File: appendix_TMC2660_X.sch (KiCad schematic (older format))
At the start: 56 parts, among them J601 Conn_01x04, J602 Conn_01x04, J603 Conn_01x04, J604 Conn_01x04, U601 TMC2660, U602 TMC2660, U603 TMC2660, U604 TMC2660

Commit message: started layouting TMC2660
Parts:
- added C633, C634, C635, C636: 470u, Capacitors_SMD:CP_Elec_6.3x5.3, symbol Device:CP
- C601, C604, C607, C608, C609, C610, C611, C612, C613, C614, C615, C616, C617, C620, C623, C624, C625, C626, C627, C628, C629, C630, C631, C632: footprint Capacitors_SMD:C_0805 -> Capacitors_SMD:C_0603
- C602, C603, C605, C606, C618, C619, C621, C622: footprint Capacitors_SMD:C_0805 -> Capacitors_SMD:C_1210
- J601, J602, J603, J604: value Conn_01x04 -> B4B-XH-A; footprint Connector_PinHeader_2.54mm:PinHeader_1x04_P2.54mm_Vertical -> Connector_JST:JST_XH_B4B-XH-A_1x04_P2.50mm_Vertical
- R601, R603, R605, R607, R609, R611, R613, R615: footprint Resistors_SMD:R_0805 -> Resistors_SMD:R_0603
- R602, R604, R606, R608, R610, R612, R614, R616: footprint Resistors_SMD:R_0805 -> Resistors_SMD:R_1210
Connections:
- wire segments 348 -> 364
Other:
- moved on the sheet: J602

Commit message: Layout: all TMC / Schematic: Oli's comments
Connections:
- net labels added: +24V, +3.3V
- net labels removed: +12V
- wire segments 364 -> 372

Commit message: added footprints, layouted 3v3 Reg
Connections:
- net D_INT_TMC_STALL_X: now reaches U602.38 (SG_TST)
- net D_INT_TMC_STALL_Y: now reaches U601.38 (SG_TST)
- net D_INT_TMC_STALL_Z1: now reaches U604.38 (SG_TST)
- net D_INT_TMC_STALL_E1: now reaches U603.38 (SG_TST)
- no-connect marks 0 -> 4

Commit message: added LEDs
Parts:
- C633, C634, C635, C636: footprint Capacitors_SMD:CP_Elec_6.3x5.3 -> Capacitor_SMD:CP_Elec_10x10
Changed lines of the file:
@@
 F 0 "C634" H 6568 1296 50  0000 L CNN
 F 1 "470u" H 6568 1205 50  0000 L CNN
-F 2 "Capacitors_SMD:CP_Elec_6.3x5.3" H 6488 1100 50  0001 C CNN
+F 2 "Capacitor_SMD:CP_Elec_10x10" H 6488 1100 50  0001 C CNN
 F 3 "~" H 6450 1250 50  0001 C CNN
 	1    6450 1250
@@
 F 0 "C633" H 13518 1246 50  0000 L CNN
 F 1 "470u" H 13518 1155 50  0000 L CNN
-F 2 "Capacitors_SMD:CP_Elec_6.3x5.3" H 13438 1050 50  0001 C CNN
+F 2 "Capacitor_SMD:CP_Elec_10x10" H 13438 1050 50  0001 C CNN
 F 3 "~" H 13400 1200 50  0001 C CNN
 	1    13400 1200
@@
 F 0 "C636" H 13518 5946 50  0000 L CNN
 F 1 "470u" H 13518 5855 50  0000 L CNN
-F 2 "Capacitors_SMD:CP_Elec_6.3x5.3" H 13438 5750 50  0001 C CNN
+F 2 "Capacitor_SMD:CP_Elec_10x10" H 13438 5750 50  0001 C CNN
 F 3 "~" H 13400 5900 50  0001 C CNN
 	1    13400 5900
@@
 F 0 "C635" H 6568 5946 50  0000 L CNN
 F 1 "470u" H 6568 5855 50  0000 L CNN
-F 2 "Capacitors_SMD:CP_Elec_6.3x5.3" H 6488 5750 50  0001 C CNN
+F 2 "Capacitor_SMD:CP_Elec_10x10" H 6488 5750 50  0001 C CNN
 F 3 "~" H 6450 5900 50  0001 C CNN
 	1    6450 5900

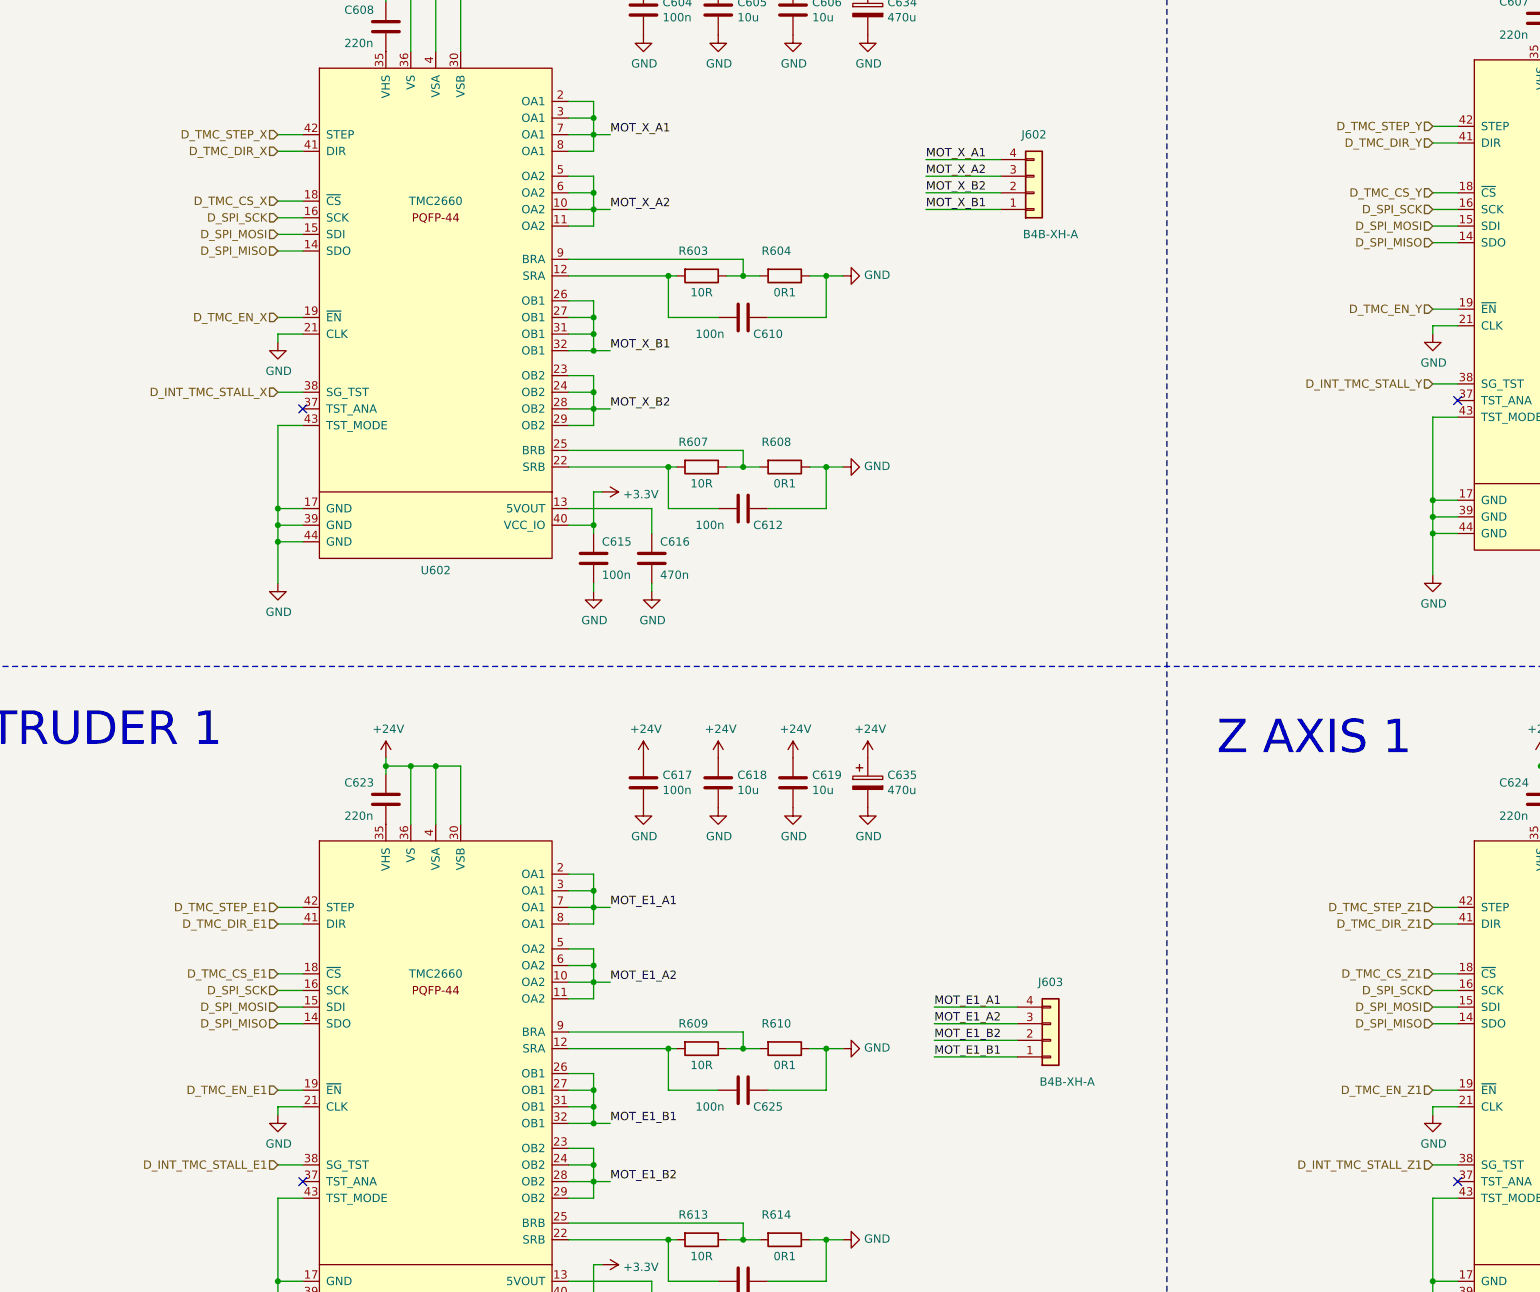
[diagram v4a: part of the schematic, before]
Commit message: started with STM32 Pinout connections (Mittagspause)
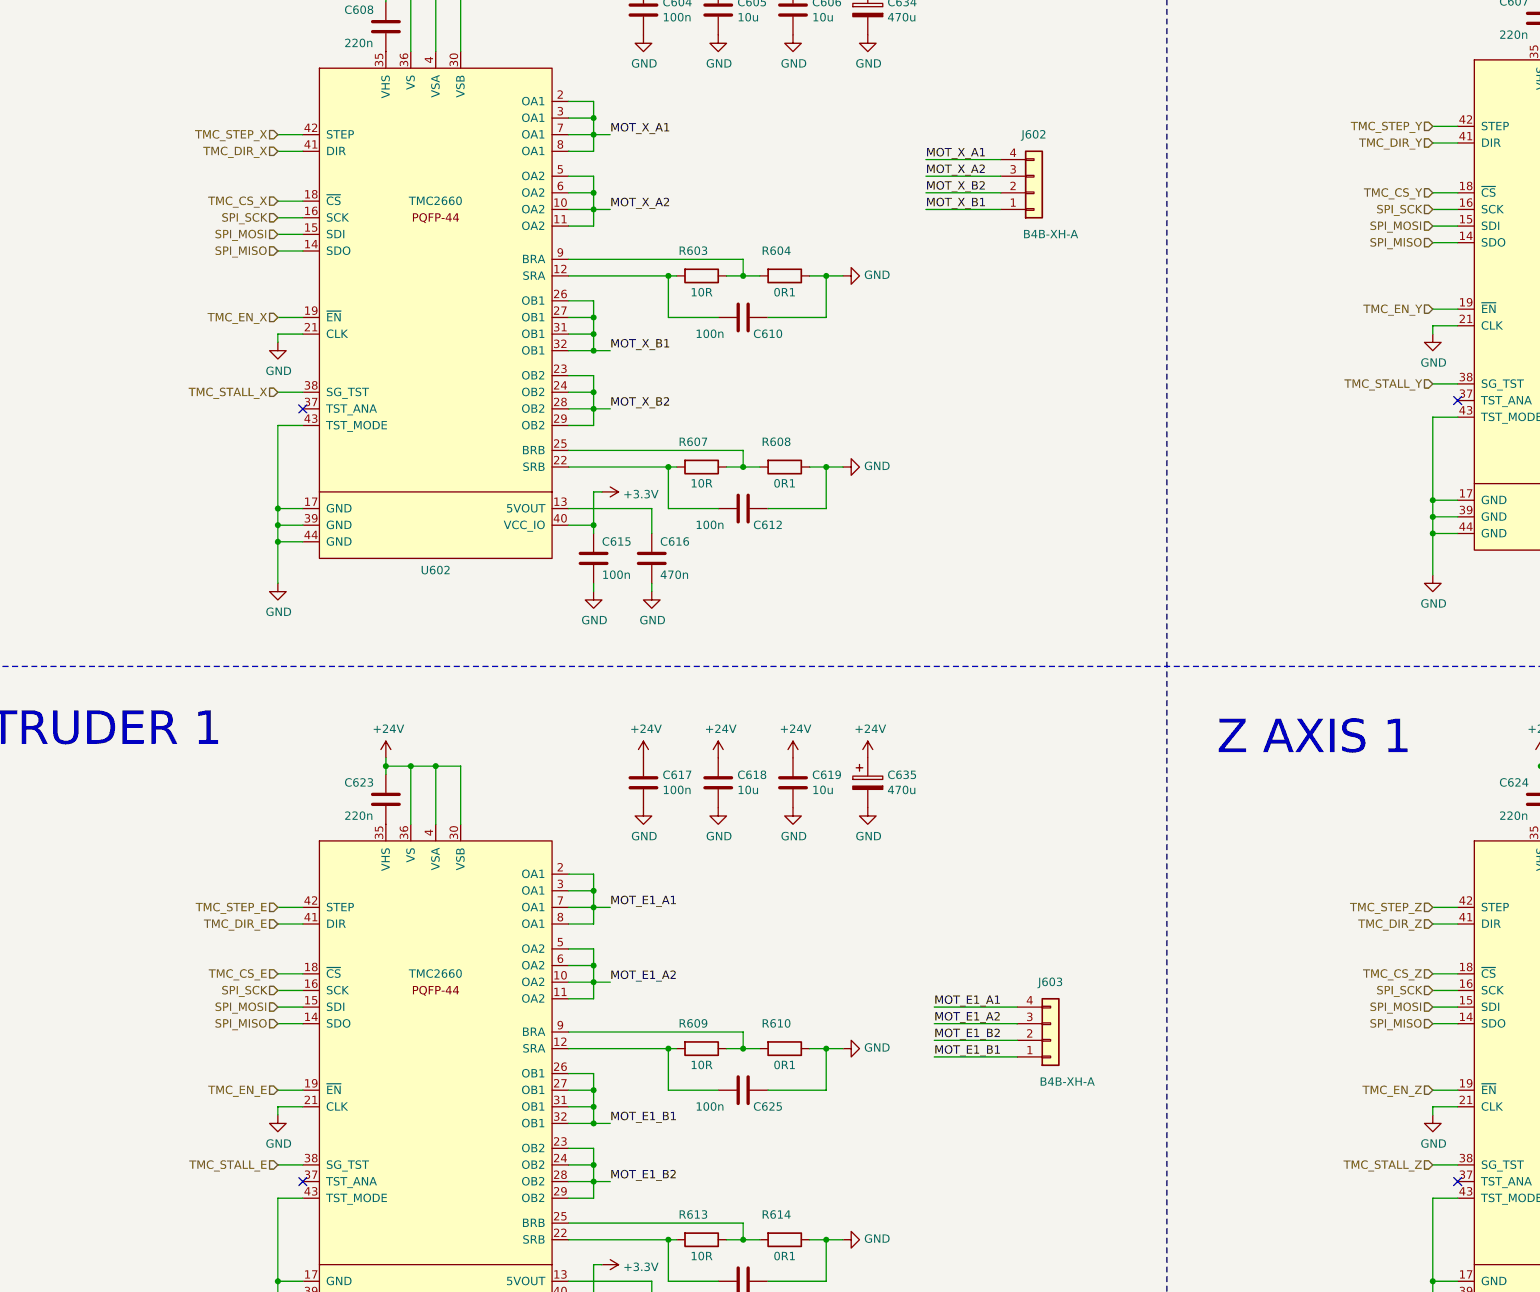
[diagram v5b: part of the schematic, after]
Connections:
- net D_INT_TMC_STALL_E1 renamed TMC_STALL_E
- net D_INT_TMC_STALL_X renamed TMC_STALL_X
- net D_INT_TMC_STALL_Y renamed TMC_STALL_Y
- net D_INT_TMC_STALL_Z1 renamed TMC_STALL_Z
- net D_SPI_MISO renamed SPI_MISO
- net D_SPI_MOSI renamed SPI_MOSI
- net D_SPI_SCK renamed SPI_SCK
- net D_TMC_CS_E1 renamed TMC_CS_E
- net D_TMC_CS_X renamed TMC_CS_X
- net D_TMC_CS_Y renamed TMC_CS_Y
- net D_TMC_CS_Z1 renamed TMC_CS_Z
- net D_TMC_DIR_E1 renamed TMC_DIR_E
- net D_TMC_DIR_X renamed TMC_DIR_X
- net D_TMC_DIR_Y renamed TMC_DIR_Y
- net D_TMC_DIR_Z1 renamed TMC_DIR_Z
- net D_TMC_EN_E1 renamed TMC_EN_E
- net D_TMC_EN_X renamed TMC_EN_X
- net D_TMC_EN_Y renamed TMC_EN_Y
- net D_TMC_EN_Z1 renamed TMC_EN_Z
- net D_TMC_STEP_E1 renamed TMC_STEP_E
- net D_TMC_STEP_X renamed TMC_STEP_X
- net D_TMC_STEP_Y renamed TMC_STEP_Y
- net D_TMC_STEP_Z1 renamed TMC_STEP_Z
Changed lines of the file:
@@
 $Descr A3 16535 11693
 encoding utf-8
-Sheet 6 6
+Sheet 5 6
 Title "TMC2660 Stepper Drivers"
 Date ""
@@
 Wire Wire Line
 	3550 1150 3550 1100
-Text HLabel 2900 3100 0    50   Input ~ 0
-D_TMC_EN_X
 Wire Wire Line
 	3050 3750 2900 3750
@@
 	2900 3750 2900 4250
 Connection ~ 2900 4250
-Text HLabel 2900 2400 0    50   Input ~ 0
-D_TMC_CS_X
-Text HLabel 2900 2500 0    50   Input ~ 0
-D_SPI_SCK
-Text HLabel 2900 2600 0    50   Input ~ 0
-D_SPI_MOSI
-Text HLabel 2900 2700 0    50   Input ~ 0
-D_SPI_MISO
 Wire Wire Line
 	2900 2400 3050 2400
@@
 Wire Wire Line
 	2900 3200 3050 3200
-Text HLabel 2900 2000 0    50   Input ~ 0
-D_TMC_STEP_X
 Wire Wire Line
 	2900 2000 3050 2000
-Text HLabel 2900 2100 0    50   Input ~ 0
-D_TMC_DIR_X
 Wire Wire Line
 	2900 2100 3050 2100
@@
 	1    0    0    -1
 $EndComp
-Text HLabel 9850 3050 0    50   Input ~ 0
-D_TMC_EN_Y
 Wire Wire Line
 	10000 3700 9850 3700
@@
 	9850 3700 9850 4200
 Connection ~ 9850 4200
-Text HLabel 9850 2350 0    50   Input ~ 0
-D_TMC_CS_Y
-Text HLabel 9850 2450 0    50   Input ~ 0
-D_SPI_SCK
-Text HLabel 9850 2550 0    50   Input ~ 0
-D_SPI_MOSI
-Text HLabel 9850 2650 0    50   Input ~ 0
-D_SPI_MISO
 Wire Wire Line
 	9850 2350 10000 2350
@@
 Wire Wire Line
 	9850 3150 10000 3150
-Text HLabel 9850 1950 0    50   Input ~ 0
-D_TMC_STEP_Y
 Wire Wire Line
 	9850 1950 10000 1950
-Text HLabel 9850 2050 0    50   Input ~ 0
-D_TMC_DIR_Y
 Wire Wire Line
 	9850 2050 10000 2050
@@
 	1    0    0    -1
 $EndComp
-Text HLabel 9850 7750 0    50   Input ~ 0
-D_TMC_EN_Z1
 Wire Wire Line
 	10000 8400 9850 8400
@@
 	9850 8400 9850 8900
 Connection ~ 9850 8900
-Text HLabel 9850 7050 0    50   Input ~ 0
-D_TMC_CS_Z1
-Text HLabel 9850 7150 0    50   Input ~ 0
-D_SPI_SCK
-Text HLabel 9850 7250 0    50   Input ~ 0
-D_SPI_MOSI
-Text HLabel 9850 7350 0    50   Input ~ 0
-D_SPI_MISO
 Wire Wire Line
 	9850 7050 10000 7050
@@
 Wire Wire Line
 	9850 7850 10000 7850
-Text HLabel 9850 6650 0    50   Input ~ 0
-D_TMC_STEP_Z1
 Wire Wire Line
 	9850 6650 10000 6650
-Text HLabel 9850 6750 0    50   Input ~ 0
-D_TMC_DIR_Z1
 Wire Wire Line
 	9850 6750 10000 6750
@@
 	1    0    0    -1
 $EndComp
-Text HLabel 2900 7750 0    50   Input ~ 0
-D_TMC_EN_E1
 Wire Wire Line
 	3050 8400 2900 8400
@@
 	2900 8400 2900 8900
 Connection ~ 2900 8900
-Text HLabel 2900 7050 0    50   Input ~ 0
-D_TMC_CS_E1
-Text HLabel 2900 7150 0    50   Input ~ 0
-D_SPI_SCK
-Text HLabel 2900 7250 0    50   Input ~ 0
-D_SPI_MOSI
-Text HLabel 2900 7350 0    50   Input ~ 0
-D_SPI_MISO
 Wire Wire Line
 	2900 7050 3050 7050
@@
 Wire Wire Line
 	2900 7850 3050 7850
-Text HLabel 2900 6650 0    50   Input ~ 0
-D_TMC_STEP_E1
 Wire Wire Line
 	2900 6650 3050 6650
-Text HLabel 2900 6750 0    50   Input ~ 0
-D_TMC_DIR_E1
 Wire Wire Line
 	2900 6750 3050 6750
@@
 EndData
 $EndBitmap
-Text HLabel 2900 3550 0    50   Input ~ 0
-D_INT_TMC_STALL_X
 Wire Wire Line
 	3050 3550 2900 3550
 NoConn ~ 3050 3650
-Text HLabel 9850 3500 0    50   Input ~ 0
-D_INT_TMC_STALL_Y
 $Comp
 L FHNW-Pro4E-FS19T8-Library:TMC2660 U601
@@
 Wire Wire Line
 	10000 3500 9850 3500
-Text HLabel 9850 8200 0    50   Input ~ 0
-D_INT_TMC_STALL_Z1
 Wire Wire Line
 	9850 8200 10000 8200
 NoConn ~ 10000 8300
-Text HLabel 2900 8200 0    50   Input ~ 0
-D_INT_TMC_STALL_E1
 NoConn ~ 3050 8300
 Wire Wire Line
 	3050 8200 2900 8200
+Text HLabel 2900 2500 0    50   Input ~ 0
+SPI_SCK
+Text HLabel 2900 2700 0    50   Input ~ 0
+SPI_MISO
+Text HLabel 2900 2600 0    50   Input ~ 0
+SPI_MOSI
+Text HLabel 9850 2450 0    50   Input ~ 0
+SPI_SCK
+Text HLabel 9850 2650 0    50   Input ~ 0
+SPI_MISO
+Text HLabel 9850 2550 0    50   Input ~ 0
+SPI_MOSI
+Text HLabel 9850 7150 0    50   Input ~ 0
+SPI_SCK
+Text HLabel 9850 7350 0    50   Input ~ 0
+SPI_MISO
+Text HLabel 9850 7250 0    50   Input ~ 0
+SPI_MOSI
+Text HLabel 2900 7150 0    50   Input ~ 0
+SPI_SCK
+Text HLabel 2900 7350 0    50   Input ~ 0
+SPI_MISO
+Text HLabel 2900 7250 0    50   Input ~ 0
+SPI_MOSI
+Text HLabel 2900 2100 0    50   Input ~ 0
+TMC_DIR_X
+Text HLabel 2900 2000 0    50   Input ~ 0
+TMC_STEP_X
+Text HLabel 2900 2400 0    50   Input ~ 0
+TMC_CS_X
+Text HLabel 2900 3100 0    50   Input ~ 0
+TMC_EN_X
+Text HLabel 9850 2050 0    50   Input ~ 0
+TMC_DIR_Y
+Text HLabel 9850 1950 0    50   Input ~ 0
+TMC_STEP_Y
+Text HLabel 9850 2350 0    50   Input ~ 0
+TMC_CS_Y
+Text HLabel 9850 6750 0    50   Input ~ 0
+TMC_DIR_Z
+Text HLabel 9850 6650 0    50   Input ~ 0
+TMC_STEP_Z
+Text HLabel 9850 7050 0    50   Input ~ 0
+TMC_CS_Z
+Text HLabel 2900 6750 0    50   Input ~ 0
+TMC_DIR_E
+Text HLabel 2900 6650 0    50   Input ~ 0
+TMC_STEP_E
+Text HLabel 2900 7050 0    50   Input ~ 0
+TMC_CS_E
+Text HLabel 9850 3050 0    50   Input ~ 0
+TMC_EN_Y
+Text HLabel 9850 7750 0    50   Input ~ 0
+TMC_EN_Z
+Text HLabel 2900 7750 0    50   Input ~ 0
+TMC_EN_E
+Text HLabel 2900 3550 0    50   Input ~ 0
+TMC_STALL_X
+Text HLabel 2900 8200 0    50   Input ~ 0
+TMC_STALL_E
+Text HLabel 9850 8200 0    50   Input ~ 0
+TMC_STALL_Z
+Text HLabel 9850 3500 0    50   Input ~ 0
+TMC_STALL_Y
 $EndSCHEMATC

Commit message: cleaned up Layout
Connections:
- net +3V3 renamed +3.3VP
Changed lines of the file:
@@
 	1    0    0    -1
-$EndComp
-$Comp
-L power:+3.3V #PWR0616
-U 1 1 5CBCCCD5
-P 4850 4150
-F 0 "#PWR0616" H 4850 4000 50  0001 C CNN
-F 1 "+3.3V" V 4865 4278 50  0000 L CNN
-F 2 "" H 4850 4150 50  0001 C CNN
-F 3 "" H 4850 4150 50  0001 C CNN
-	1    4850 4150
-	0    1    1    0
 $EndComp
 Connection ~ 4800 4350
@@
 Wire Wire Line
 	4800 4150 4800 4350
-$Comp
-L power:+3.3V #PWR0627
-U 1 1 5CBF990E
-P 4850 8800
-F 0 "#PWR0627" H 4850 8650 50  0001 C CNN
-F 1 "+3.3V" V 4865 8928 50  0000 L CNN
-F 2 "" H 4850 8800 50  0001 C CNN
-F 3 "" H 4850 8800 50  0001 C CNN
-	1    4850 8800
-	0    1    1    0
-$EndComp
 Wire Wire Line
 	4850 8800 4800 8800
 Wire Wire Line
 	4800 8800 4800 9000
-$Comp
-L power:+3.3V #PWR0628
-U 1 1 5CC988AA
-P 11800 8800
-F 0 "#PWR0628" H 11800 8650 50  0001 C CNN
-F 1 "+3.3V" V 11815 8928 50  0000 L CNN
-F 2 "" H 11800 8800 50  0001 C CNN
-F 3 "" H 11800 8800 50  0001 C CNN
-	1    11800 8800
-	0    1    1    0
-$EndComp
 Wire Wire Line
 	11800 8800 11750 8800
 Wire Wire Line
 	11750 8800 11750 9000
-$Comp
-L power:+3.3V #PWR0615
-U 1 1 5CCC268B
-P 11800 4100
-F 0 "#PWR0615" H 11800 3950 50  0001 C CNN
-F 1 "+3.3V" V 11815 4228 50  0000 L CNN
-F 2 "" H 11800 4100 50  0001 C CNN
-F 3 "" H 11800 4100 50  0001 C CNN
-	1    11800 4100
-	0    1    1    0
-$EndComp
 Wire Wire Line
 	11800 4100 11750 4100
@@
 Text HLabel 9850 3500 0    50   Input ~ 0
 TMC_STALL_Y
+$Comp
+L power:+3.3VP #PWR?
+U 1 1 5CD5617D
+P 4850 8800
+AR Path="/5CD5617D" Ref="#PWR?"  Part="1"
+AR Path="/5CA3FF44/5CD5617D" Ref="#PWR0174"  Part="1"
+F 0 "#PWR0174" H 5000 8750 50  0001 C CNN
+F 1 "+3.3VP" V 4850 9050 50  0000 C CNN
+F 2 "" H 4850 8800 50  0001 C CNN
+F 3 "" H 4850 8800 50  0001 C CNN
+	1    4850 8800
+	0    1    1    0
+$EndComp
+$Comp
+L power:+3.3VP #PWR?
+U 1 1 5CD7FEC9
+P 11800 8800
+AR Path="/5CD7FEC9" Ref="#PWR?"  Part="1"
+AR Path="/5CA3FF44/5CD7FEC9" Ref="#PWR0181"  Part="1"
+F 0 "#PWR0181" H 11950 8750 50  0001 C CNN
+F 1 "+3.3VP" V 11800 9050 50  0000 C CNN
+F 2 "" H 11800 8800 50  0001 C CNN
+F 3 "" H 11800 8800 50  0001 C CNN
+	1    11800 8800
+	0    1    1    0
+$EndComp
+$Comp
+L power:+3.3VP #PWR?
+U 1 1 5CD810F3
+P 11800 4100
+AR Path="/5CD810F3" Ref="#PWR?"  Part="1"
+AR Path="/5CA3FF44/5CD810F3" Ref="#PWR0185"  Part="1"
+F 0 "#PWR0185" H 11950 4050 50  0001 C CNN
+F 1 "+3.3VP" V 11800 4350 50  0000 C CNN
+F 2 "" H 11800 4100 50  0001 C CNN
+F 3 "" H 11800 4100 50  0001 C CNN
+	1    11800 4100
+	0    1    1    0
+$EndComp
+$Comp
+L power:+3.3VP #PWR?
+U 1 1 5CD82494
+P 4850 4150
+AR Path="/5CD82494" Ref="#PWR?"  Part="1"
+AR Path="/5CA3FF44/5CD82494" Ref="#PWR0186"  Part="1"
+F 0 "#PWR0186" H 5000 4100 50  0001 C CNN
+F 1 "+3.3VP" V 4850 4400 50  0000 C CNN
+F 2 "" H 4850 4150 50  0001 C CNN
+F 3 "" H 4850 4150 50  0001 C CNN
+	1    4850 4150
+	0    1    1    0
+$EndComp
 $EndSCHEMATC
